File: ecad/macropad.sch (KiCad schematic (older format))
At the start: 50 parts

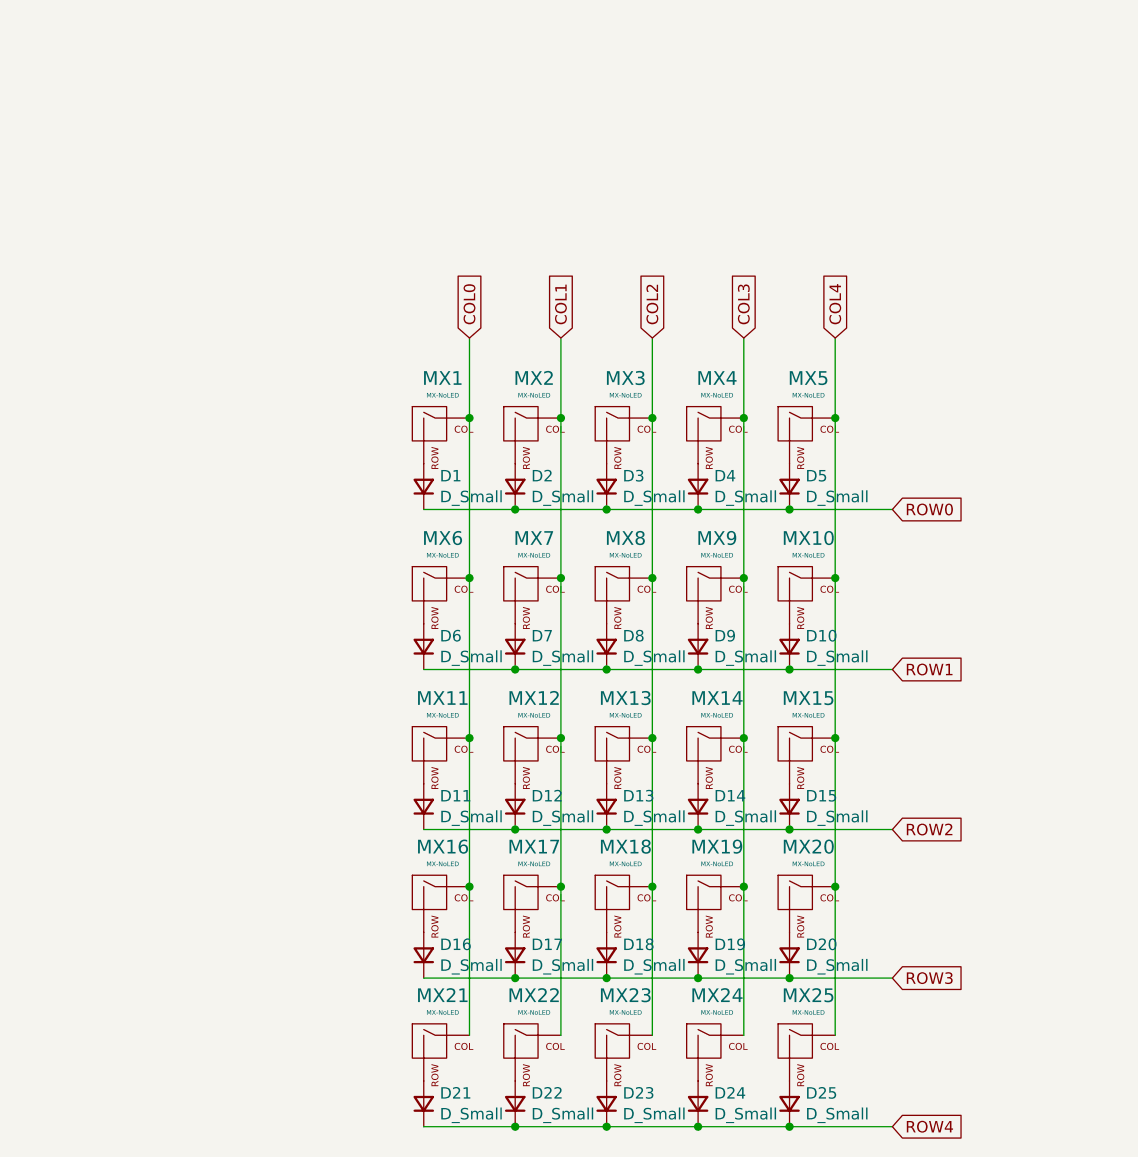
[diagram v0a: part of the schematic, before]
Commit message: Placed macropad into a box ins sch
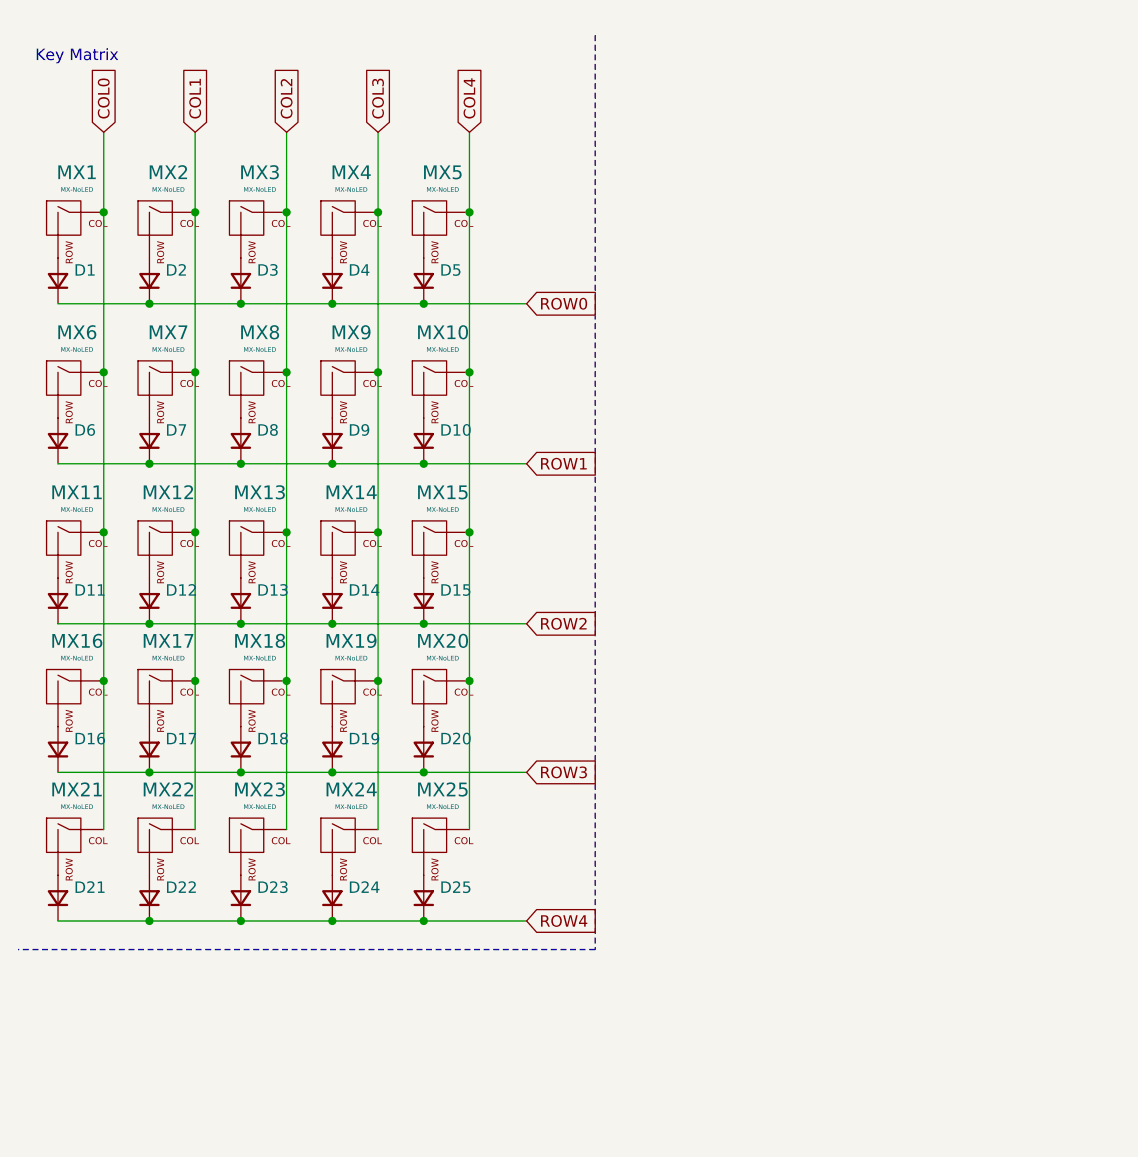
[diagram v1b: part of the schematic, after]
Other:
- note added: "Key Matrix"
- moved on the sheet: D1, D10, D11, D12, D13, D14, D15, D16, D17, D18, D19, D2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
